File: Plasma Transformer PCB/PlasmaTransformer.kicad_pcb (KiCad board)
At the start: 2 copper layers, 90 x 90 mm, 99 parts, among them J1 Barrel_Jack_MountingPin, J10 Conn_01x01_Socket, J11 Screw_Terminal_01x01, J12 Screw_Terminal_01x01, J13 Conn_01x01_Socket, J14 Conn_01x01_Socket, J15 Conn_01x01_Socket, J16 Conn_01x01_Socket, J17 Conn_01x01_Socket, J18 Conn_01x01_Socket, J19 Conn_01x01_Socket, J2 Conn_01x02_Pin, J20 Conn_01x01_Socket, J21 Conn_01x01_Socket, J3 Conn_Coaxial, J4 Conn_02x04_Odd_Even, J5 Conn_Coaxial, J6 Conn_02x04_Odd_Even, J7 Conn_01x01_Socket, J8 AudioJack3, J9 Conn_01x01_Socket, M1 Fan, Q1 Q_NMOS_Depletion_GDS, SW1 SW_SPDT, T1 BO-02, T2 ZS 1052-S HT(H), U1 LMR51610YDBVR, U2 TLV9302IDDFR

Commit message: manufacturing cleanup
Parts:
- U2: footprint ALibrary:SOT-23-8-Soldermask-Defined -> Package_SO:SOIC-8_3.9x4.9mm_P1.27mm
- moved C11 2.10 mm to (85.1, 58.5)
- moved C31 2.10 mm to (85.1, 66.3)
- moved R14 2.10 mm to (85.1, 62.4)
- moved R16 2.10 mm to (85.1, 64.3)
- moved R3 2.10 mm to (85.1, 56.5)
- moved R4 2.10 mm to (85.1, 60.5)
- moved RV1 2.10 mm to (80.9, 60.0)
- moved R5 1.94 mm to (91.9, 67.6)
- moved U2 1.48 mm to (92.2, 63.6)
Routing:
- net /GND-IN: track 43.4 -> 45.7 mm, vias 1 -> 2
- net Net-(C11-Pad2): track 45.6 -> 47.8 mm
- net Net-(U2A--): track 14.8 -> 13.1 mm, vias 2 -> 0
- net Net-(U2A-+): track 7.36 -> 5.75 mm
- net /REF10V: track 10.4 -> 11.9 mm
- net Net-(U2B--): track 2.56 -> 3.84 mm
- net Net-(U2B-+): track 2.06 -> 2.80 mm
- net +12V: track 113.0 -> 112.4 mm
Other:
- board text added: "REV 6 | JUL 2026 | E. CHIU"
- board text removed: "REV 6 | NOV 2025 | E. CHIU"

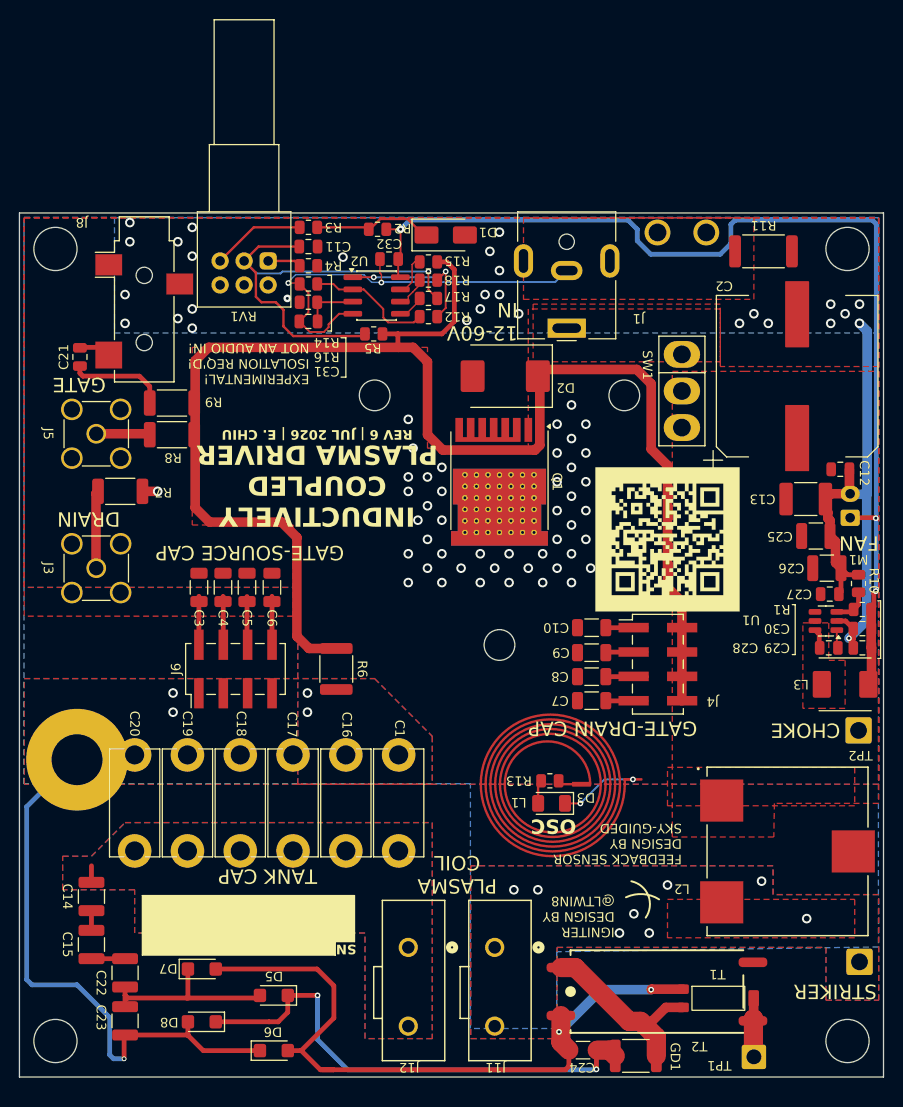
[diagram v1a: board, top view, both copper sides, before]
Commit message: updated hole size for press-fit capacitor sockets
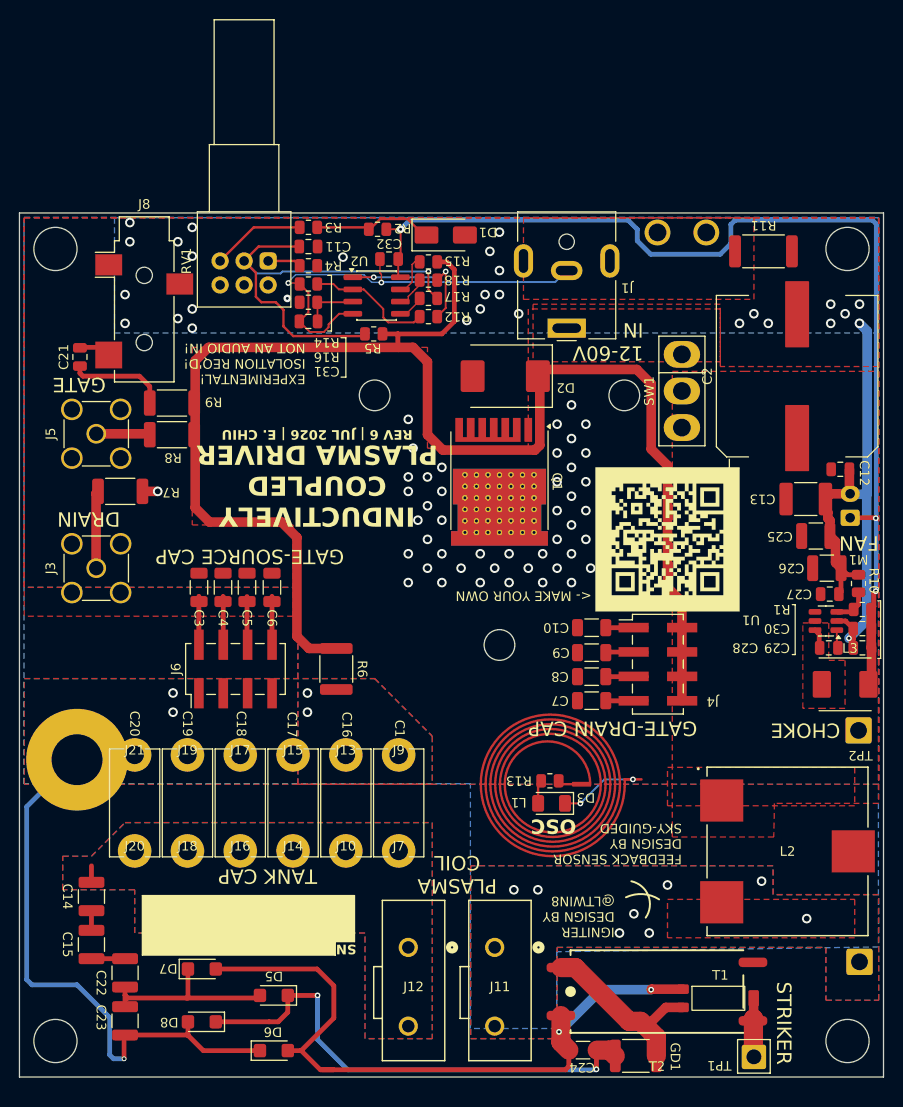
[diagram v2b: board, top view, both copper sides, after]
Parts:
- C2: footprint ALibrary:CP_Elec_16x17.5_FK_Series -> AFootprints:CP_Elec_16x17.5_FK_Series
- J10, J13, J14, J15, J16, J17, J18, J19, J20, J21, J7, J9: footprint ALibrary:H8501-05 -> AFootprints:H8501-05
- J11, J12: footprint ALibrary:CONN_2604-3101_WAG -> AFootprints:CONN_2604-3101_WAG
- J3, J5: footprint ALibrary:SMA_Amphenol_901-144_Vertical -> AFootprints:SMA_Amphenol_901-144_Vertical
- J8: footprint ALibrary:Jack_3.5mm_CUI_SJ-3523-SMT_Horizontal -> AFootprints:Jack_3.5mm_CUI_SJ-3523-SMT_Horizontal
- L2: footprint ALibrary:B82559B_TDK -> AFootprints:B82559B_TDK
- L3: footprint ALibrary:L_Pana_PCC-KVP_5.5x5mm -> AFootprints:L_Pana_PCC-KVP_5.5x5mm
- RV1: footprint ALibrary:Bourns-Potentiometer-PTD902-2 -> AFootprints:Bourns-Potentiometer-PTD902-2
- SW1: footprint ALibrary:CKSW-E101J1AV2QE2 -> AFootprints:CKSW-E101J1AV2QE2
- T1: footprint ALibrary:BO-02 -> AFootprints:BO-02
- T2: footprint ALibrary:ZS 1052-S HT(H) -> AFootprints:ZS 1052-S HT(H)
- U2: value TLV9302IDDFR -> TLV9302IDR
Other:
- board text added: "<- MAKE YOUR OWN"
